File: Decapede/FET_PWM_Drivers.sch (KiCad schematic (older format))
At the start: 40 parts, among them J12 FET1_PWM, J13 FET2_PWM, J14 FET3_PWM, J15 FET4_PWM, Q17 BC817-25,215, Q18 BC817-25,215, Q19 PSMN023-40YLCX, Q20 PSMN023-40YLCX, Q21 BC807,215, Q22 BC807,215, Q23 BC817-25,215, Q24 BC817-25,215, Q25 PSMN023-40YLCX, Q26 PSMN023-40YLCX, Q27 BC807,215, Q28 BC807,215

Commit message: Updates for Decapede project.
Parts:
- removed D11, D9: Diode 10TQ035, ~, symbol DIODESCH
- added D11, D13, D20, D9: LED, ~, symbol LED
- added D14, D21: ES1D, ~, symbol DIODESCH
- D10, D12: value Diode 10TQ035 -> ES1D
- J12: value FET1_PWM -> FET6
- J13: value FET2_PWM -> FET7
- J14: value FET3_PWM -> FET8
- J15: value FET4_PWM -> FET9
- Q19, Q20, Q25, Q26: symbol BUK7226-75A -> PSMN023-40YLCX
- R75, R78, R85, R88: value 30 Ohm -> 1k8
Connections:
- net +12V: now also R75.1, R78.1, R85.1, R88.1
- net +24V: now also D10.2 (K), D12.2 (K), D14.2 (K), D21.2 (K)
- net FET1_PWM: now also R77.1
- net FET2_PWM: now also R80.1
- net FET3_PWM: now also R87.1
- net FET4_PWM: now also R90.1
- net GND: now also Q19.1 (S), Q20.1 (S), Q25.1 (S), Q26.1 (S); no longer D10.1 (A), D12.1 (A), Q19.3 (S), Q20.3 (S), Q25.3 (S), Q26.3 (S)
- net at Q21.2 (E), R76.2: no longer R75.2
- net FET_OUT_P1: now reaches J12.2 (PM)
- net FET_OUT_P1: now also D10.1 (A), Q19.5 (D), D9.2 (K); no longer Q19.2 (D)
- net at Q22.2 (E), R79.2: no longer R78.2
- net FET_OUT_P2: now reaches J13.2 (PM)
- net FET_OUT_P2: now also D12.1 (A), Q20.5 (D), D11.2 (K); no longer Q20.2 (D)
- net at Q27.2 (E), R86.2: no longer R85.2
- net FET_OUT_P3: now reaches J14.2 (PM)
- net FET_OUT_P3: now also Q25.5 (D), D20.2 (K), D21.1 (A); no longer Q25.2 (D)
- net at Q28.2 (E), R89.2: no longer R88.2
- net FET_OUT_P4: now reaches J15.2 (PM)
- net FET_OUT_P4: now also Q26.5 (D), D13.2 (K), D14.1 (A); no longer Q26.2 (D)
- new net: Q19.4 (G), R71.2, R76.1
- new net: Q20.4 (G), R72.2, R79.1
- new net: Q25.4 (G), R81.2, R86.1
- new net: Q26.4 (G), R82.2, R89.1
- new net: D9.1 (A), R75.2
- new net: D11.1 (A), R78.2
- new net: D20.1 (A), R88.2
- new net: D13.1 (A), R85.2
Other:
- moved on the sheet: J14, Q23, Q25, Q27, R77, R81, R83, R86, R87, R90

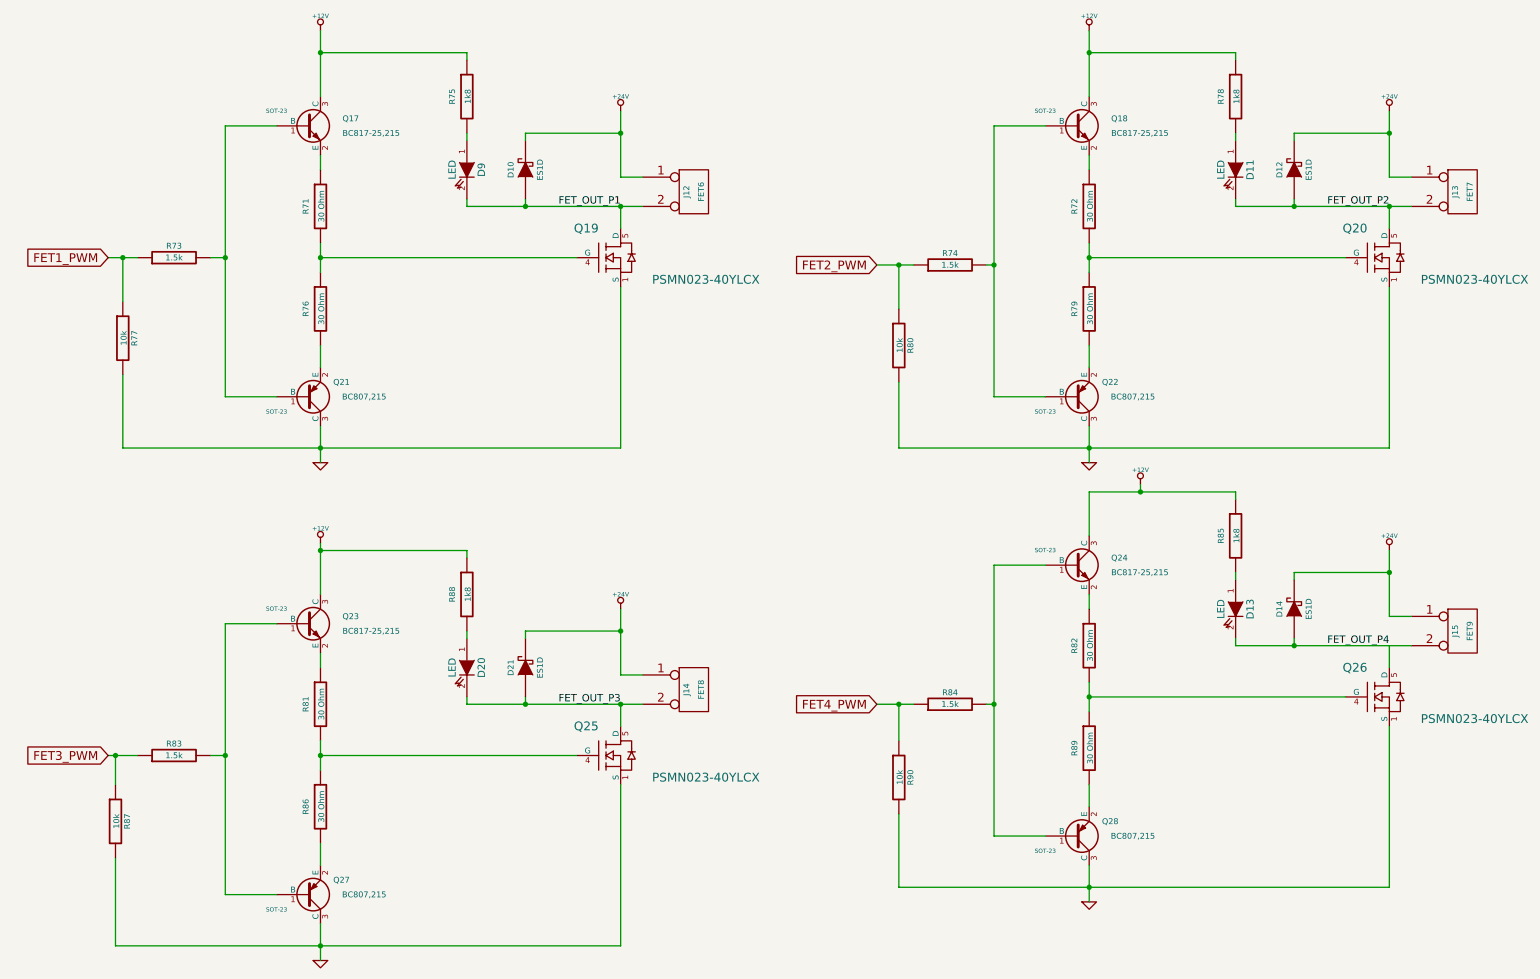
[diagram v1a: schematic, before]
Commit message: Decapede update: add fuses for each main section; change endstops to use 0V instead of 5V; more space for stepper drivers to allow latching connectors
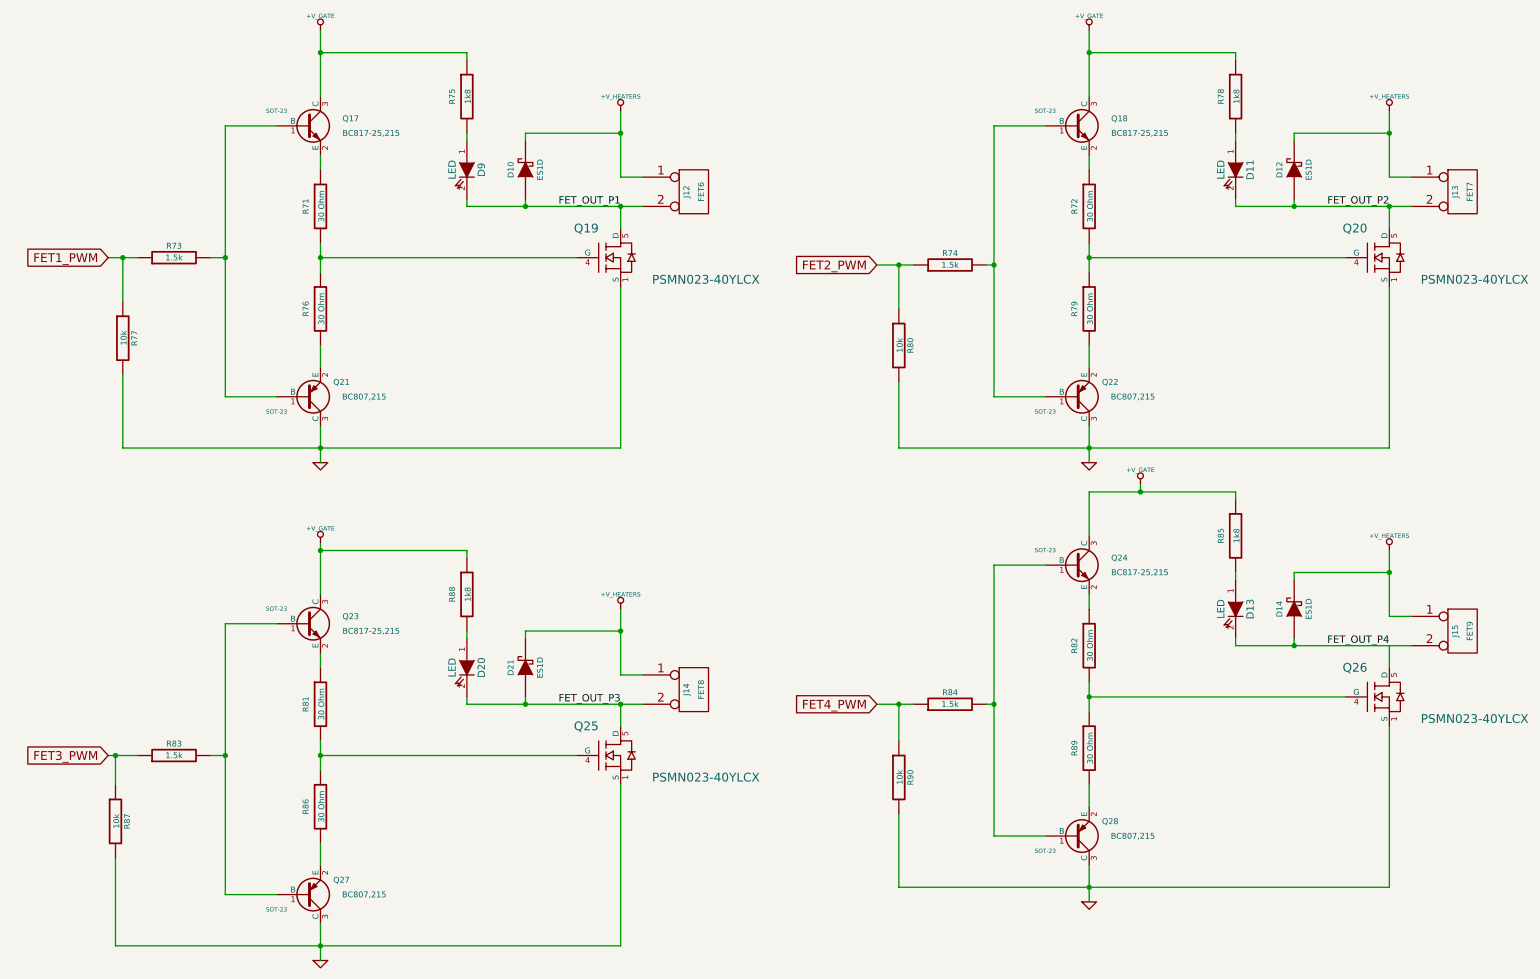
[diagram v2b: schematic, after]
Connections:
- net +12V renamed +V_GATE
- net +24V renamed +V_HEATERS
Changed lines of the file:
@@
 Sheet 7 10
 Title "FET-PWM Driver Stage"
-Date "26 jan 2014"
+Date "30 jan 2014"
 Rev ""
 Comp ""
@@
 $EndComp
 $Comp
-L +12V #PWR0143
-U 1 1 52DC2895
-P 2400 750
-F 0 "#PWR0143" H 2400 700 20  0001 C CNN
-F 1 "+12V" H 2400 850 30  0000 C CNN
-F 2 "" H 2400 750 60  0000 C CNN
-F 3 "" H 2400 750 60  0000 C CNN
-	1    2400 750
-	1    0    0    -1
-$EndComp
-$Comp
-L GND #PWR0144
+L GND #PWR0147
 U 1 1 52DC289B
 P 2400 3700
-F 0 "#PWR0144" H 2400 3700 30  0001 C CNN
+F 0 "#PWR0147" H 2400 3700 30  0001 C CNN
 F 1 "GND" H 2400 3630 30  0001 C CNN
 F 2 "" H 2400 3700 60  0000 C CNN
@@
 F 3 "" H 4950 1850 60  0000 C CNN
 	1    4950 1850
-	1    0    0    -1
-$EndComp
-$Comp
-L +24V #PWR0145
-U 1 1 52DC28CF
-P 4450 1300
-F 0 "#PWR0145" H 4450 1250 20  0001 C CNN
-F 1 "+24V" H 4450 1400 30  0000 C CNN
-F 2 "" H 4450 1300 60  0000 C CNN
-F 3 "" H 4450 1300 60  0000 C CNN
-	1    4450 1300
 	1    0    0    -1
 $EndComp
@@
 $EndComp
 $Comp
-L +12V #PWR0146
-U 1 1 52DC290D
-P 7650 750
-F 0 "#PWR0146" H 7650 700 20  0001 C CNN
-F 1 "+12V" H 7650 850 30  0000 C CNN
-F 2 "" H 7650 750 60  0000 C CNN
-F 3 "" H 7650 750 60  0000 C CNN
-	1    7650 750
-	1    0    0    -1
-$EndComp
-$Comp
-L GND #PWR0147
+L GND #PWR0148
 U 1 1 52DC2913
 P 7650 3700
-F 0 "#PWR0147" H 7650 3700 30  0001 C CNN
+F 0 "#PWR0148" H 7650 3700 30  0001 C CNN
 F 1 "GND" H 7650 3630 30  0001 C CNN
 F 2 "" H 7650 3700 60  0000 C CNN
@@
 F 3 "" H 10200 1850 60  0000 C CNN
 	1    10200 1850
-	1    0    0    -1
-$EndComp
-$Comp
-L +24V #PWR0148
-U 1 1 52DC2948
-P 9700 1300
-F 0 "#PWR0148" H 9700 1250 20  0001 C CNN
-F 1 "+24V" H 9700 1400 30  0000 C CNN
-F 2 "" H 9700 1300 60  0000 C CNN
-F 3 "" H 9700 1300 60  0000 C CNN
-	1    9700 1300
 	1    0    0    -1
 $EndComp
@@
 $EndComp
 $Comp
-L +12V #PWR0149
-U 1 1 52DC2986
-P 2400 4250
-F 0 "#PWR0149" H 2400 4200 20  0001 C CNN
-F 1 "+12V" H 2400 4350 30  0000 C CNN
-F 2 "" H 2400 4250 60  0000 C CNN
-F 3 "" H 2400 4250 60  0000 C CNN
-	1    2400 4250
-	1    0    0    -1
-$EndComp
-$Comp
-L GND #PWR0150
+L GND #PWR0149
 U 1 1 52DC298C
 P 2400 7100
-F 0 "#PWR0150" H 2400 7100 30  0001 C CNN
+F 0 "#PWR0149" H 2400 7100 30  0001 C CNN
 F 1 "GND" H 2400 7030 30  0001 C CNN
 F 2 "" H 2400 7100 60  0000 C CNN
@@
 F 3 "" H 4950 5250 60  0000 C CNN
 	1    4950 5250
-	1    0    0    -1
-$EndComp
-$Comp
-L +24V #PWR0151
-U 1 1 52DC29C0
-P 4450 4700
-F 0 "#PWR0151" H 4450 4650 20  0001 C CNN
-F 1 "+24V" H 4450 4800 30  0000 C CNN
-F 2 "" H 4450 4700 60  0000 C CNN
-F 3 "" H 4450 4700 60  0000 C CNN
-	1    4450 4700
 	1    0    0    -1
 $EndComp
@@
 $EndComp
 $Comp
-L +12V #PWR0152
-U 1 1 52DC29FE
-P 8000 3850
-F 0 "#PWR0152" H 8000 3800 20  0001 C CNN
-F 1 "+12V" H 8000 3950 30  0000 C CNN
-F 2 "" H 8000 3850 60  0000 C CNN
-F 3 "" H 8000 3850 60  0000 C CNN
-	1    8000 3850
-	1    0    0    -1
-$EndComp
-$Comp
-L GND #PWR0153
+L GND #PWR0150
 U 1 1 52DC2A04
 P 7650 6700
-F 0 "#PWR0153" H 7650 6700 30  0001 C CNN
+F 0 "#PWR0150" H 7650 6700 30  0001 C CNN
 F 1 "GND" H 7650 6630 30  0001 C CNN
 F 2 "" H 7650 6700 60  0000 C CNN
@@
 F 3 "" H 10200 4850 60  0000 C CNN
 	1    10200 4850
-	1    0    0    -1
-$EndComp
-$Comp
-L +24V #PWR0154
-U 1 1 52DC2A39
-P 9700 4300
-F 0 "#PWR0154" H 9700 4250 20  0001 C CNN
-F 1 "+24V" H 9700 4400 30  0000 C CNN
-F 2 "" H 9700 4300 60  0000 C CNN
-F 3 "" H 9700 4300 60  0000 C CNN
-	1    9700 4300
 	1    0    0    -1
 $EndComp
@@
 	7650 3900 8650 3900
 Connection ~ 9700 4450
+$Comp
+L +V_HEATERS #PWR0151
+U 1 1 52E836C9
+P 4450 1300
+F 0 "#PWR0151" H 4450 1270 30  0001 C CNN
+F 1 "+V_HEATERS" H 4450 1400 30  0000 C CNN
+F 2 "~" H 4450 1300 60  0000 C CNN
+F 3 "~" H 4450 1300 60  0000 C CNN
+	1    4450 1300
+	1    0    0    -1
+$EndComp
+$Comp
+L +V_HEATERS #PWR0152
+U 1 1 52E836D8
+P 9700 1300
+F 0 "#PWR0152" H 9700 1270 30  0001 C CNN
+F 1 "+V_HEATERS" H 9700 1400 30  0000 C CNN
+F 2 "~" H 9700 1300 60  0000 C CNN
+F 3 "~" H 9700 1300 60  0000 C CNN
+	1    9700 1300
+	1    0    0    -1
+$EndComp
+$Comp
+L +V_HEATERS #PWR0153
+U 1 1 52E836E7
+P 9700 4300
+F 0 "#PWR0153" H 9700 4270 30  0001 C CNN
+F 1 "+V_HEATERS" H 9700 4400 30  0000 C CNN
+F 2 "~" H 9700 4300 60  0000 C CNN
+F 3 "~" H 9700 4300 60  0000 C CNN
+	1    9700 4300
+	1    0    0    -1
+$EndComp
+$Comp
+L +V_HEATERS #PWR0154
+U 1 1 52E836F6
+P 4450 4700
+F 0 "#PWR0154" H 4450 4670 30  0001 C CNN
+F 1 "+V_HEATERS" H 4450 4800 30  0000 C CNN
+F 2 "~" H 4450 4700 60  0000 C CNN
+F 3 "~" H 4450 4700 60  0000 C CNN
+	1    4450 4700
+	1    0    0    -1
+$EndComp
+$Comp
+L +V_GATE #PWR0155
+U 1 1 52E83705
+P 2400 4250
+F 0 "#PWR0155" H 2400 4220 30  0001 C CNN
+F 1 "+V_GATE" H 2400 4350 30  0000 C CNN
+F 2 "~" H 2400 4250 60  0000 C CNN
+F 3 "~" H 2400 4250 60  0000 C CNN
+	1    2400 4250
+	1    0    0    -1
+$EndComp
+$Comp
+L +V_GATE #PWR0156
+U 1 1 52E83714
+P 2400 750
+F 0 "#PWR0156" H 2400 720 30  0001 C CNN
+F 1 "+V_GATE" H 2400 850 30  0000 C CNN
+F 2 "~" H 2400 750 60  0000 C CNN
+F 3 "~" H 2400 750 60  0000 C CNN
+	1    2400 750
+	1    0    0    -1
+$EndComp
+$Comp
+L +V_GATE #PWR0157
+U 1 1 52E83723
+P 7650 750
+F 0 "#PWR0157" H 7650 720 30  0001 C CNN
+F 1 "+V_GATE" H 7650 850 30  0000 C CNN
+F 2 "~" H 7650 750 60  0000 C CNN
+F 3 "~" H 7650 750 60  0000 C CNN
+	1    7650 750
+	1    0    0    -1
+$EndComp
+$Comp
+L +V_GATE #PWR0158
+U 1 1 52E83732
+P 8000 3850
+F 0 "#PWR0158" H 8000 3820 30  0001 C CNN
+F 1 "+V_GATE" H 8000 3950 30  0000 C CNN
+F 2 "~" H 8000 3850 60  0000 C CNN
+F 3 "~" H 8000 3850 60  0000 C CNN
+	1    8000 3850
+	1    0    0    -1
+$EndComp
 $EndSCHEMATC
